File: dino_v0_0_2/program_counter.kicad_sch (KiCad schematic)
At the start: 20 parts, among them U1 74LS193, U10 74LS02, U11 74LS245, U12 74LS245, U13 74LS245, U14 74LS245, U2 74LS193, U3 74LS193, U36 7400, U4 74LS193

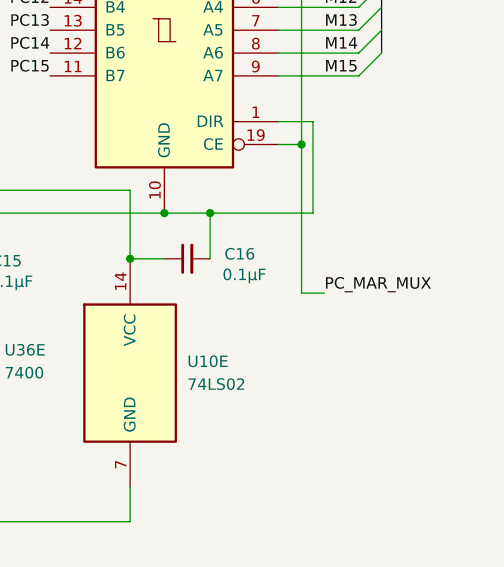
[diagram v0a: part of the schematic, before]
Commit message: feat(dino): complete v0.0.3 schematic — all 11 sheets netlist-clean
- wire MAR sheet: '373 LO/HI latches, 2x '245 M-bus drive, A15 decode
  (ROM_EN/~RAM_EN), LE stamps off /MAR_LO_LOAD//MAR_HI_LOAD
- fix PC_MAR_MUX polarity: PC '245s enabled on bit14=0, inverted vs
  bit-map convention (PC=1); add ~PC_MAR_MUX inverter, relabel U13/U14
- wire all 7 control-word bus taps [15:9] (SA0-2, END, PC_UP,
  PC_MAR_MUX, HALT) — label pairs had no wire between them
- untie NONE/NC '138 outputs: totem-pole bus fight on every microword;
  each unused output now individually no_connect
- build END (U61 NOR: ~MR = RESET|END, sync T-state clear) and HALT
  (T-state freeze via CET, clock keeps running)
- build COND/JNZ (U62: ~PC_LOAD = taken-JNZ | unconditional-JMP)
- claim src code 111 as /SW_OUT: IN port — DIP switches through 10k
  pull-ups onto W bus via '244; LED bank active-high off OB0-7
- add U66 missing power unit + decouplers (C63-C66)
- tools: kicad_gen_sheet.py (declarative YAML/JSON sheet generator,
  deterministic uuid5, collision-checked), kicad_xsheet_audit.py
  (cross-sheet contract audit); archive stale testing-strategy doc
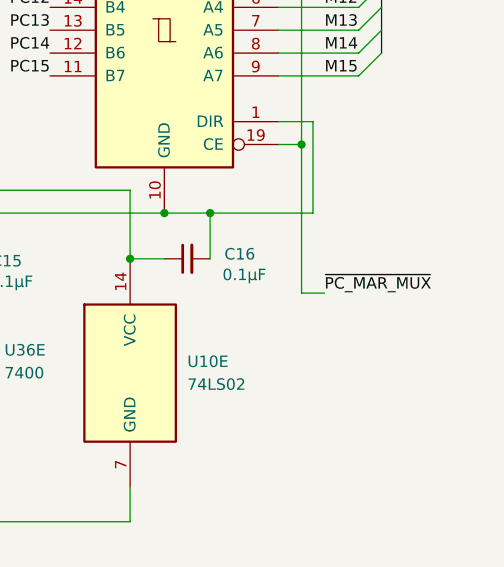
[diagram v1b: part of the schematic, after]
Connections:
- net PC_MAR_MUX renamed ~{PC_MAR_MUX}
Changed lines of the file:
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@@
 		)
 	)
-	(label "PC_MAR_MUX"
+	(label "~{PC_MAR_MUX}"
 		(at 254 119.38 0)
 		(effects
